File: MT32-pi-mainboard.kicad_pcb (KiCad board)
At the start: 2 copper layers, 100 x 100 mm, 23 parts, among them J1 RPi, J2 MIDI In, J3 LCD2004, J4 5V, J5 LCD2004, SW1 Encoder, SW2 Button 1, SW3 Button 2, SW4 Power, U1 6N138

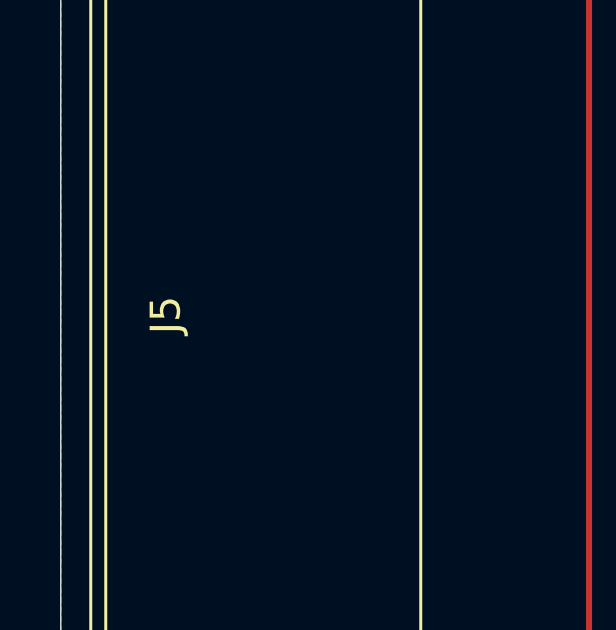
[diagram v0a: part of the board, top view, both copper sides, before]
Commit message: add symbols for virtual models and graphics
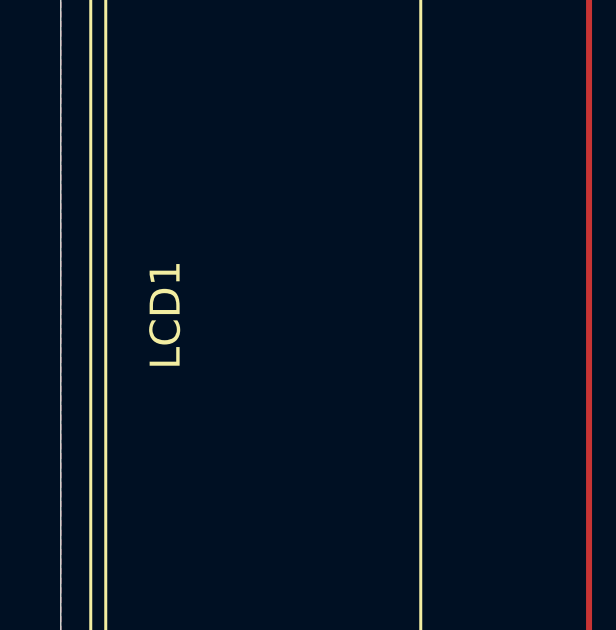
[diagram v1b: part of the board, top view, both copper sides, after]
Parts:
- removed G*** (x2): LOGO, 0:crankery_small
- removed G***: LOGO, 0:mt32-pi-logo
- removed J5: LCD2004, 0:LCD2004
- added G1: mt32-pi logo, 0:mt32-pi-logo, B.Cu at (101.7, 98.2)
- added G2: Crankery Logo, 0:crankery_small, F.Cu at (144.7, 139.1)
- added G3: Crankery Logo, 0:crankery_small, B.Cu at (100.7, 108.8)
- added LCD1: LCD2004, 0:LCD2004, F.Cu at (62.3, 70.4)

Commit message: cleanup, add gerbers
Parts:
- D1: footprint Diode_THT:D_DO-35_SOD27_P7.62mm_Horizontal -> 0:D_DO-35_SOD27_P7.62mm_Horizontal
- J3: footprint Connector_PinSocket_2.54mm:PinSocket_1x16_P2.54mm_Horizontal -> 0:PinSocket_1x16_P2.54mm_Horizontal
- R1, R2, R3: footprint Resistor_THT:R_Axial_DIN0207_L6.3mm_D2.5mm_P7.62mm_Horizontal -> 0:R_Axial_DIN0207_L6.3mm_D2.5mm_P7.62mm_Horizontal
- U1: footprint Package_DIP:DIP-8_W7.62mm -> 0:DIP-8_W7.62mm
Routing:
- net +5V: track 64.6 -> 63.1 mm
- net DAC_{BCK}: track 68.0 -> 68.7 mm
- net DAC_{LCK}: track 107.7 -> 107.1 mm

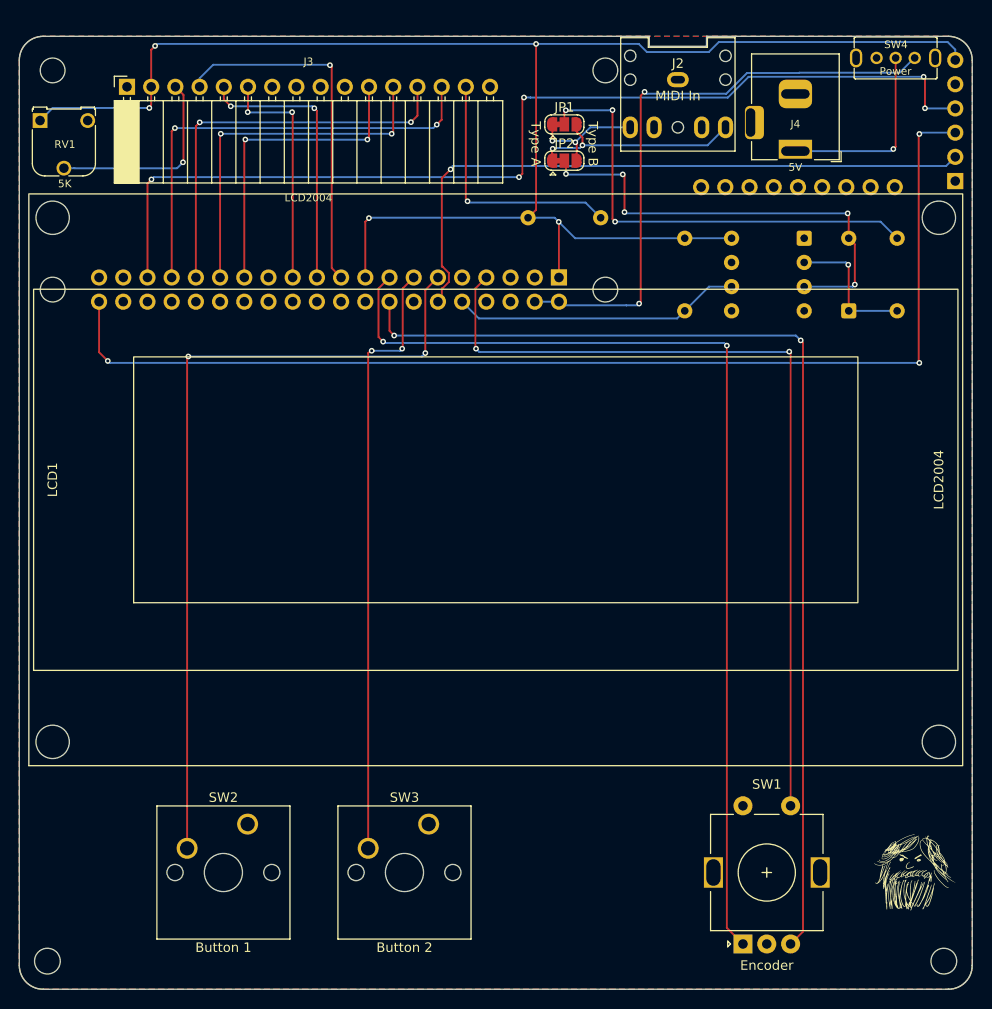
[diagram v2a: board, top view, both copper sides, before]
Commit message: clean up silks, use project properties for text
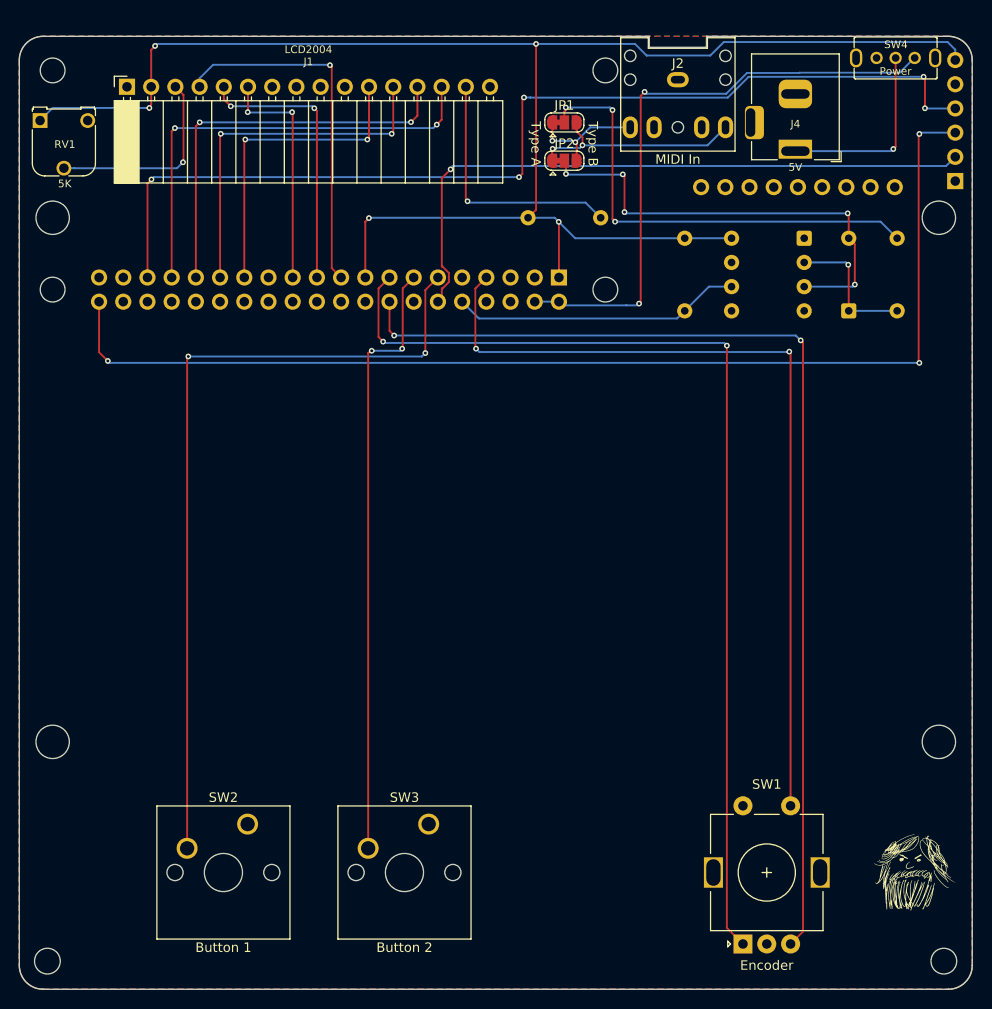
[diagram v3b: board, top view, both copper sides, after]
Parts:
- RP1: renamed from J1; value RPi -> Raspberry Pi Zero 2 W
- moved JP1 0.20 mm to (108.2, 60.4)
- renumbered A1 to DAC1, J3 to J1
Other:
- board text added: "${Title} Board layout by ${Author} (${Company}) ${Github} Rev ${Revision} (${Issue_Date}) Thanks to https://github.com/dwhinham/mt32-pi for all the hard work"
- board text removed: "All credit goes to https://github.com/dwhinham/mt32-pi Board layout by Dave Hamilton https://github.com/crankery/mt32-pi-mainboard 2026-02-16"

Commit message: regenerate gerbers
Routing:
- net DAC_{BCK}: track 68.7 -> 68.1 mm
